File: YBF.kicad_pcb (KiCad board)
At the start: 2 copper layers, 173.9 x 130.1 mm, 119 parts, among them J1 Chain_LED_out, J2 Chain_LED_return, SW1 1825910-6, SW2 1825910-6

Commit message: Hieracrchical PCB
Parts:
- removed the C1 at (119.9, 134.1)
- removed the C3 at (46.5, 157.5)
- removed the C4 at (46.5, 160.0)
- removed the C5 at (46.5, 162.6)
- removed the C6 at (46.5, 165.1)
- removed the C7 at (46.5, 167.6)
- removed the C8 at (46.5, 170.2)
- added C100: 1uF, Capacitor_SMD:C_0603_1608Metric, F.Cu at (32.8, 260.4)
- added C101: 1uF, Capacitor_SMD:C_0603_1608Metric, F.Cu at (1.03, 236.2)
- added C102: 1uF, Capacitor_SMD:C_0603_1608Metric, F.Cu at (45.2, 260.4)
- added C103: 1uF, Capacitor_SMD:C_0603_1608Metric, F.Cu at (57.9, 252.2)
- added C104: 1uF, Capacitor_SMD:C_0603_1608Metric, F.Cu at (20.1, 260.4)
- added C53: 1uF, Capacitor_SMD:C_0603_1608Metric, F.Cu at (20.1, 220.0)
- added C54: 1uF, Capacitor_SMD:C_0603_1608Metric, F.Cu at (51.6, 228.1)
- added C55: 1uF, Capacitor_SMD:C_0603_1608Metric, F.Cu at (1.03, 260.4)
- added C56: 1uF, Capacitor_SMD:C_0603_1608Metric, F.Cu at (39.1, 252.2)
- added C57: 1uF, Capacitor_SMD:C_0603_1608Metric, F.Cu at (1.03, 276.4)
- added C58: 1uF, Capacitor_SMD:C_0603_1608Metric, F.Cu at (39.1, 244.1)
- added C59: 1uF, Capacitor_SMD:C_0603_1608Metric, F.Cu at (39.1, 268.5)
- added C60: 1uF, Capacitor_SMD:C_0603_1608Metric, F.Cu at (7.38, 284.5)
- added C61: 1uF, Capacitor_SMD:C_0603_1608Metric, F.Cu at (45.2, 220.0)
- added C62: 1uF, Capacitor_SMD:C_0603_1608Metric, F.Cu at (20.1, 236.2)
- added C63: 1uF, Capacitor_SMD:C_0603_1608Metric, F.Cu at (7.38, 228.1)
- added C64: 1uF, Capacitor_SMD:C_0603_1608Metric, F.Cu at (51.6, 276.4)
- added C65: 1uF, Capacitor_SMD:C_0603_1608Metric, F.Cu at (20.1, 268.5)
- added C66: 1uF, Capacitor_SMD:C_0603_1608Metric, F.Cu at (26.4, 252.2)
- added C67: 1uF, Capacitor_SMD:C_0603_1608Metric, F.Cu at (1.03, 252.2)
- added C68: 1uF, Capacitor_SMD:C_0603_1608Metric, F.Cu at (26.4, 260.4)
- added C69: 1uF, Capacitor_SMD:C_0603_1608Metric, F.Cu at (13.7, 260.4)
- added C70: 1uF, Capacitor_SMD:C_0603_1608Metric, F.Cu at (7.38, 260.4)
- added C71: 1uF, Capacitor_SMD:C_0603_1608Metric, F.Cu at (1.03, 220.0)
- added C72: 1uF, Capacitor_SMD:C_0603_1608Metric, F.Cu at (57.9, 268.5)
- added C73: 1uF, Capacitor_SMD:C_0603_1608Metric, F.Cu at (20.1, 244.1)
- added C74: 1uF, Capacitor_SMD:C_0603_1608Metric, F.Cu at (7.38, 276.4)
- added C75: 1uF, Capacitor_SMD:C_0603_1608Metric, F.Cu at (7.38, 236.2)
- added C76: 1uF, Capacitor_SMD:C_0603_1608Metric, F.Cu at (39.1, 260.4)
- added C77: 1uF, Capacitor_SMD:C_0603_1608Metric, F.Cu at (51.6, 244.1)
- added C78: 1uF, Capacitor_SMD:C_0603_1608Metric, F.Cu at (32.8, 244.1)
- added C79: 1uF, Capacitor_SMD:C_0603_1608Metric, F.Cu at (45.2, 252.2)
- added C80: 1uF, Capacitor_SMD:C_0603_1608Metric, F.Cu at (20.1, 228.1)
- added C81: 1uF, Capacitor_SMD:C_0603_1608Metric, F.Cu at (7.38, 268.5)
- added C82: 1uF, Capacitor_SMD:C_0603_1608Metric, F.Cu at (64.3, 236.2)
- added C83: 1uF, Capacitor_SMD:C_0603_1608Metric, F.Cu at (1.03, 228.1)
- added C84: 1uF, Capacitor_SMD:C_0603_1608Metric, F.Cu at (39.1, 236.2)
- added C85: 1uF, Capacitor_SMD:C_0603_1608Metric, F.Cu at (32.8, 276.4)
- added C86: 1uF, Capacitor_SMD:C_0603_1608Metric, F.Cu at (1.03, 244.1)
- added C87: 1uF, Capacitor_SMD:C_0603_1608Metric, F.Cu at (51.6, 260.4)
- added C88: 1uF, Capacitor_SMD:C_0603_1608Metric, F.Cu at (45.2, 284.5)
- added C89: 1uF, Capacitor_SMD:C_0603_1608Metric, F.Cu at (51.6, 236.2)
- added C90: 1uF, Capacitor_SMD:C_0603_1608Metric, F.Cu at (45.2, 228.1)
- added C91: 1uF, Capacitor_SMD:C_0603_1608Metric, F.Cu at (64.3, 268.5)
- added C92: 1uF, Capacitor_SMD:C_0603_1608Metric, F.Cu at (45.2, 268.5)
- added C93: 1uF, Capacitor_SMD:C_0603_1608Metric, F.Cu at (26.4, 228.1)
- added C94: 1uF, Capacitor_SMD:C_0603_1608Metric, F.Cu at (13.7, 276.4)
- added C95: 1uF, Capacitor_SMD:C_0603_1608Metric, F.Cu at (1.03, 284.5)
- added C96: 1uF, Capacitor_SMD:C_0603_1608Metric, F.Cu at (51.6, 220.0)
- added C97: 1uF, Capacitor_SMD:C_0603_1608Metric, F.Cu at (45.2, 236.2)
- added C98: 1uF, Capacitor_SMD:C_0603_1608Metric, F.Cu at (39.1, 228.1)
- added C99: 1uF, Capacitor_SMD:C_0603_1608Metric, F.Cu at (13.7, 236.2)
- added D2: WS2812B-2020, LED_SMD:LED_WS2812B-2020_PLCC4_2.0x2.0mm, F.Cu at (124.0, 152.4)
- added D53: WS2812B-2020, LED_SMD:LED_WS2812B-2020_PLCC4_2.0x2.0mm, F.Cu at (45.2, 222.2)
- added D54: WS2812B-2020, LED_SMD:LED_WS2812B-2020_PLCC4_2.0x2.0mm, F.Cu at (20.1, 238.5)
- added D55: WS2812B-2020, LED_SMD:LED_WS2812B-2020_PLCC4_2.0x2.0mm, F.Cu at (7.37, 230.4)
- added D56: WS2812B-2020, LED_SMD:LED_WS2812B-2020_PLCC4_2.0x2.0mm, F.Cu at (51.6, 278.6)
- added D57: WS2812B-2020, LED_SMD:LED_WS2812B-2020_PLCC4_2.0x2.0mm, F.Cu at (20.1, 270.8)
- added D58: WS2812B-2020, LED_SMD:LED_WS2812B-2020_PLCC4_2.0x2.0mm, F.Cu at (26.4, 254.5)
- added D59: WS2812B-2020, LED_SMD:LED_WS2812B-2020_PLCC4_2.0x2.0mm, F.Cu at (1.02, 254.5)
- added D60: WS2812B-2020, LED_SMD:LED_WS2812B-2020_PLCC4_2.0x2.0mm, F.Cu at (26.4, 262.6)
- added D61: WS2812B-2020, LED_SMD:LED_WS2812B-2020_PLCC4_2.0x2.0mm, F.Cu at (13.7, 262.6)
- added D62: WS2812B-2020, LED_SMD:LED_WS2812B-2020_PLCC4_2.0x2.0mm, F.Cu at (7.37, 262.6)
- added D63: WS2812B-2020, LED_SMD:LED_WS2812B-2020_PLCC4_2.0x2.0mm, F.Cu at (1.02, 222.2)
- added D64: WS2812B-2020, LED_SMD:LED_WS2812B-2020_PLCC4_2.0x2.0mm, F.Cu at (57.9, 270.8)
- added D65: WS2812B-2020, LED_SMD:LED_WS2812B-2020_PLCC4_2.0x2.0mm, F.Cu at (20.1, 246.4)
- added D66: WS2812B-2020, LED_SMD:LED_WS2812B-2020_PLCC4_2.0x2.0mm, F.Cu at (7.37, 278.6)
- added D67: WS2812B-2020, LED_SMD:LED_WS2812B-2020_PLCC4_2.0x2.0mm, F.Cu at (7.37, 238.5)
- added D68: WS2812B-2020, LED_SMD:LED_WS2812B-2020_PLCC4_2.0x2.0mm, F.Cu at (39.1, 262.6)
- added D69: WS2812B-2020, LED_SMD:LED_WS2812B-2020_PLCC4_2.0x2.0mm, F.Cu at (51.6, 246.4)
- added D70: WS2812B-2020, LED_SMD:LED_WS2812B-2020_PLCC4_2.0x2.0mm, F.Cu at (32.8, 246.4)
- added D71: WS2812B-2020, LED_SMD:LED_WS2812B-2020_PLCC4_2.0x2.0mm, F.Cu at (45.2, 254.5)
- added D72: WS2812B-2020, LED_SMD:LED_WS2812B-2020_PLCC4_2.0x2.0mm, F.Cu at (20.1, 230.4)
- added D73: WS2812B-2020, LED_SMD:LED_WS2812B-2020_PLCC4_2.0x2.0mm, F.Cu at (7.37, 270.8)
- added D74: WS2812B-2020, LED_SMD:LED_WS2812B-2020_PLCC4_2.0x2.0mm, F.Cu at (64.3, 238.5)
- added D75: WS2812B-2020, LED_SMD:LED_WS2812B-2020_PLCC4_2.0x2.0mm, F.Cu at (1.02, 230.4)
- added D76: WS2812B-2020, LED_SMD:LED_WS2812B-2020_PLCC4_2.0x2.0mm, F.Cu at (39.1, 238.5)
- added D77: WS2812B-2020, LED_SMD:LED_WS2812B-2020_PLCC4_2.0x2.0mm, F.Cu at (32.8, 278.6)
- added D78: WS2812B-2020, LED_SMD:LED_WS2812B-2020_PLCC4_2.0x2.0mm, F.Cu at (1.02, 246.4)
- added D79: WS2812B-2020, LED_SMD:LED_WS2812B-2020_PLCC4_2.0x2.0mm, F.Cu at (51.6, 262.6)
- added D80: WS2812B-2020, LED_SMD:LED_WS2812B-2020_PLCC4_2.0x2.0mm, F.Cu at (45.2, 286.8)
- added D81: WS2812B-2020, LED_SMD:LED_WS2812B-2020_PLCC4_2.0x2.0mm, F.Cu at (51.6, 238.5)
- added D82: WS2812B-2020, LED_SMD:LED_WS2812B-2020_PLCC4_2.0x2.0mm, F.Cu at (45.2, 230.4)
- added D83: WS2812B-2020, LED_SMD:LED_WS2812B-2020_PLCC4_2.0x2.0mm, F.Cu at (64.3, 270.8)
- added D84: WS2812B-2020, LED_SMD:LED_WS2812B-2020_PLCC4_2.0x2.0mm, F.Cu at (45.2, 270.8)
- added D85: WS2812B-2020, LED_SMD:LED_WS2812B-2020_PLCC4_2.0x2.0mm, F.Cu at (26.4, 230.4)
- added D86: WS2812B-2020, LED_SMD:LED_WS2812B-2020_PLCC4_2.0x2.0mm, F.Cu at (13.7, 278.6)
- added D87: WS2812B-2020, LED_SMD:LED_WS2812B-2020_PLCC4_2.0x2.0mm, F.Cu at (1.02, 286.8)
- added D88: WS2812B-2020, LED_SMD:LED_WS2812B-2020_PLCC4_2.0x2.0mm, F.Cu at (51.6, 222.2)
- added D89: WS2812B-2020, LED_SMD:LED_WS2812B-2020_PLCC4_2.0x2.0mm, F.Cu at (45.2, 238.5)
- added D90: WS2812B-2020, LED_SMD:LED_WS2812B-2020_PLCC4_2.0x2.0mm, F.Cu at (39.1, 230.4)
- added D91: WS2812B-2020, LED_SMD:LED_WS2812B-2020_PLCC4_2.0x2.0mm, F.Cu at (13.7, 238.5)
- added D92: WS2812B-2020, LED_SMD:LED_WS2812B-2020_PLCC4_2.0x2.0mm, F.Cu at (32.8, 262.6)
- added D93: WS2812B-2020, LED_SMD:LED_WS2812B-2020_PLCC4_2.0x2.0mm, F.Cu at (1.02, 238.5)
- added D94: WS2812B-2020, LED_SMD:LED_WS2812B-2020_PLCC4_2.0x2.0mm, F.Cu at (45.2, 262.6)
- added D95: WS2812B-2020, LED_SMD:LED_WS2812B-2020_PLCC4_2.0x2.0mm, F.Cu at (57.9, 254.5)
- added D96: WS2812B-2020, LED_SMD:LED_WS2812B-2020_PLCC4_2.0x2.0mm, F.Cu at (20.1, 262.6)
- moved C23 133.0 mm to (39.1, 284.5), turned to 180 degrees
- moved C14 132.2 mm to (13.7, 284.5), turned to 180 degrees
- moved C34 128.0 mm to (26.4, 276.4), turned to 180 degrees
- moved C48 128.0 mm to (32.8, 284.5), turned to 180 degrees
- moved D21 126.8 mm to (26.4, 286.8)
- moved C16 125.7 mm to (20.1, 284.5), turned to 180 degrees
- moved C15 124.5 mm to (51.6, 284.5), turned to 180 degrees
- moved D40 123.3 mm to (32.8, 286.8)
- moved D49 122.3 mm to (1.02, 278.6)
- moved C29 120.2 mm to (26.4, 284.5), turned to 180 degrees
- moved C25 118.3 mm to (13.7, 268.5), turned to 180 degrees
- moved D52 117.9 mm to (7.37, 286.8)
- moved D15 116.9 mm to (39.1, 286.8)
- moved D7 116.6 mm to (51.6, 286.8)
- moved C26 116.4 mm to (57.9, 276.4), turned to 180 degrees
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- renumbered C60 to C1, C53 to C2, C55 to C3, C59 to C4, C56 to C5, C58 to C6, C57 to C7, C54 to C8, U4 to U1, U1 to U2, U2 to U3
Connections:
- net Net-(D10-DIN) renamed /ws2812_and_cap8/DOUT
- net Net-(D10-DOUT) renamed /ws2812_and_cap10/DIN
- net Net-(D11-DOUT) renamed /ws2812_and_cap10/DOUT
- net Net-(D12-DOUT) renamed /ws2812_and_cap11/DOUT
- net Net-(D13-DOUT) renamed /ws2812_and_cap12/DOUT
- net Net-(D14-DOUT) renamed /ws2812_and_cap13/DOUT
- net Net-(D15-DOUT) renamed /ws2812_and_cap14/DOUT
- net Net-(D17-DOUT) renamed /ws2812_and_cap17/DOUT
- net Net-(D20-DOUT) renamed /ws2812_and_cap19/DOUT
- net Net-(D21-DOUT) renamed /ws2812_and_cap20/DOUT
- net Net-(D22-DOUT) renamed /ws2812_and_cap21/DOUT
- net Net-(D23-DOUT) renamed /ws2812_and_cap22/DOUT
- net Net-(D24-DOUT) renamed /ws2812_and_cap23/DOUT
- net Net-(D25-DOUT) renamed /ws2812_and_cap24/DOUT
- net Net-(D4-DOUT) renamed /ws2812_and_cap3/DOUT
- net Net-(D5-DOUT) renamed /ws2812_and_cap4/DOUT
- net Net-(D6-DOUT) renamed /ws2812_and_cap5/DOUT
- net Net-(D7-DOUT) renamed /ws2812_and_cap6/DOUT
- net Net-(D8-DOUT) renamed /ws2812_and_cap7/DOUT
- D1 pad 1: Net-(D1-DOUT) -> /ws2812_and_cap1/DOUT
- D1 pad 3: /Perimeter LEDs/DIN -> /ws2812_and_cap/DOUT
- D16 pad 1: Net-(D16-DOUT) -> /ws2812_and_cap15/DOUT
- D17 pad 3: Net-(D16-DOUT) -> /ws2812_and_cap16/DOUT
- D18 pad 1: Net-(D18-DOUT) -> /ws2812_and_cap18/DOUT
- D19 pad 1: Net-(D19-DOUT) -> /ws2812_and_cap16/DOUT
- D19 pad 3: Net-(D18-DOUT) -> /ws2812_and_cap15/DOUT
- D20 pad 3: Net-(D19-DOUT) -> /ws2812_and_cap18/DOUT
- D26 pad 1: Net-(D26-DOUT) -> /ws2812_and_cap25/DOUT
- D27 pad 1: Net-(D27-DOUT) -> /ws2812_and_cap26/DOUT
- D27 pad 3: Net-(D27-DIN) -> /ws2812_and_cap25/DOUT
- D28 pad 1: Net-(D27-DIN) -> /ws2812_and_cap27/DOUT
- D28 pad 3: Net-(D28-DIN) -> /ws2812_and_cap26/DOUT
- D29 pad 1: Net-(D28-DIN) -> /ws2812_and_cap28/DOUT
- D29 pad 3: Net-(D29-DIN) -> /ws2812_and_cap27/DOUT
- D3 pad 1: Net-(D3-DOUT) -> /ws2812_and_cap/DOUT
- D3 pad 3: Net-(D2-DOUT) -> PERIM_LED_DATA_IN
- D30 pad 1: Net-(D29-DIN) -> /ws2812_and_cap29/DOUT
- D30 pad 3: Net-(D30-DIN) -> /ws2812_and_cap28/DOUT
- D31 pad 1: Net-(D30-DIN) -> /ws2812_and_cap30/DOUT
- D31 pad 3: Net-(D31-DIN) -> /ws2812_and_cap29/DOUT
- D32 pad 1: Net-(D31-DIN) -> /ws2812_and_cap31/DOUT
- D32 pad 3: Net-(D32-DIN) -> /ws2812_and_cap30/DOUT
- D33 pad 1: Net-(D32-DIN) -> /ws2812_and_cap33/DOUT
- D33 pad 3: Net-(D33-DIN) -> /ws2812_and_cap32/DOUT
- D34 pad 1: Net-(D33-DIN) -> /ws2812_and_cap34/DOUT
- D34 pad 3: Net-(D34-DIN) -> /ws2812_and_cap33/DOUT
- D35 pad 1: Net-(D34-DIN) -> /ws2812_and_cap32/DOUT
- D35 pad 3: Net-(D35-DIN) -> /ws2812_and_cap31/DOUT
- D36 pad 1: Net-(D35-DIN) -> /ws2812_and_cap35/DOUT
- D36 pad 3: Net-(D36-DIN) -> /ws2812_and_cap34/DOUT
- D37 pad 1: Net-(D36-DIN) -> /ws2812_and_cap36/DOUT
- D37 pad 3: Net-(D37-DIN) -> /ws2812_and_cap35/DOUT
- D38 pad 1: Net-(D37-DIN) -> /ws2812_and_cap37/DOUT
- D38 pad 3: Net-(D38-DIN) -> /ws2812_and_cap36/DOUT
- D39 pad 1: Net-(D38-DIN) -> /ws2812_and_cap38/DOUT
- D39 pad 3: Net-(D26-DOUT) -> /ws2812_and_cap37/DOUT
- D4 pad 3: Net-(D3-DOUT) -> /ws2812_and_cap2/DOUT
- D40 pad 1: /DATA_CHAIN_OUT -> /ws2812_and_cap39/DOUT
- D40 pad 3: Net-(D40-DIN) -> /ws2812_and_cap38/DOUT
- D41 pad 1: Net-(D40-DIN) -> /ws2812_and_cap40/DOUT
- D41 pad 3: Net-(D41-DIN) -> /ws2812_and_cap39/DOUT
- D42 pad 1: Net-(D41-DIN) -> /ws2812_and_cap41/DOUT
- D42 pad 3: Net-(D42-DIN) -> /ws2812_and_cap40/DOUT
- D43 pad 1: Net-(D42-DIN) -> /ws2812_and_cap42/DOUT
- D43 pad 3: Net-(D43-DIN) -> /ws2812_and_cap41/DOUT
- D44 pad 1: Net-(D43-DIN) -> /ws2812_and_cap43/DOUT
- D44 pad 3: Net-(D44-DIN) -> /ws2812_and_cap42/DOUT
- D45 pad 1: Net-(D44-DIN) -> /ws2812_and_cap44/DOUT
- D45 pad 3: Net-(D45-DIN) -> /ws2812_and_cap43/DOUT
- D46 pad 1: Net-(D45-DIN) -> /ws2812_and_cap45/DOUT
- D46 pad 3: Net-(D46-DIN) -> /ws2812_and_cap44/DOUT
- D47 pad 1: Net-(D46-DIN) -> /ws2812_and_cap46/DOUT
- D47 pad 3: Net-(D47-DIN) -> /ws2812_and_cap45/DOUT
- D48 pad 1: Net-(D47-DIN) -> /ws2812_and_cap47/DOUT
- D48 pad 3: Net-(D48-DIN) -> /ws2812_and_cap46/DOUT
- D49 pad 1: Net-(D48-DIN) -> /ws2812_and_cap48/DOUT
- D49 pad 3: Net-(D49-DIN) -> /ws2812_and_cap47/DOUT
- D50 pad 1: Net-(D49-DIN) -> /ws2812_and_cap49/DOUT
- D50 pad 3: Net-(D50-DIN) -> /ws2812_and_cap48/DOUT
- D51 pad 1: Net-(D50-DIN) -> /ws2812_and_cap50/DOUT
- D51 pad 3: Net-(D51-DIN) -> /ws2812_and_cap49/DOUT
- D52 pad 1: Net-(D51-DIN) -> /ws2812_and_cap51/DOUT
- D52 pad 3: Net-(D27-DOUT) -> /ws2812_and_cap50/DOUT
- J1 pad 2: /DATA_CHAIN_OUT -> PERIM_LED_DATA_IN
- U2 pad 5: /Perimeter LEDs/DIN -> PERIM_LED_DATA_OUT
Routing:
- net GND: track 1.54 -> 427.6 mm, vias 0 -> 96
- net Vdrive: track 3.68 -> 171.7 mm
- net /ws2812_and_cap70/DOUT: track 0.00 -> 4.67 mm
- net /ws2812_and_cap10/DIN: track 0.00 -> 4.67 mm
- net /ws2812_and_cap84/DOUT: track 0.00 -> 4.67 mm
- net /ws2812_and_cap54/DOUT: track 0.00 -> 4.67 mm
- net /ws2812_and_cap47/DOUT: track 0.00 -> 4.67 mm
- net /ws2812_and_cap83/DOUT: track 0.00 -> 4.67 mm
- net /ws2812_and_cap65/DOUT: track 0.00 -> 4.67 mm
- net /ws2812_and_cap31/DOUT: track 0.00 -> 4.67 mm
- net /ws2812_and_cap57/DOUT: track 0.00 -> 4.67 mm
- net /ws2812_and_cap8/DOUT: track 0.00 -> 4.67 mm
- net /ws2812_and_cap24/DOUT: track 0.00 -> 4.67 mm
- net /ws2812_and_cap33/DOUT: track 0.00 -> 4.67 mm
- net /ws2812_and_cap20/DOUT: track 0.00 -> 4.67 mm
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
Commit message: place perim LEDs
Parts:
- removed C100, C101, C102, C103, C104, C79, C80, C81, C82, C83, C84, C85, C86, C87, C88, C89, C90, C91, C92, C93, C94, C95, C96, C97, C98, C99: 1uF, Capacitor_SMD:C_0603_1608Metric
- removed D71, D72, D73, D74, D75, D76, D77, D78, D79, D80, D81, D82, D83, D84, D85, D86, D87, D88, D89, D90, D91, D92, D93, D94, D95, D96: WS2812B-2020, LED_SMD:LED_WS2812B-2020_PLCC4_2.0x2.0mm
- moved C60 291.8 mm to (201.4, 66.5)
- moved D52 291.8 mm to (201.4, 68.8)
- moved D49 270.3 mm to (193.3, 88.6)
- moved C57 270.3 mm to (193.3, 86.4)
- moved C74 262.6 mm to (220.9, 123.4)
- moved D66 262.6 mm to (220.9, 125.7)
- moved D40 262.5 mm to (159.5, 56.9), turned to 180 degrees
- moved C48 258.5 mm to (159.5, 59.2), turned to 0 degrees
- moved D38 258.3 mm to (157.3, 39.8), turned to 180 degrees
- moved C42 257.6 mm to (136.5, 37.8)
- moved D34 257.6 mm to (136.4, 40.1)
- moved C46 254.5 mm to (157.3, 42.1), turned to 0 degrees
- moved C59 251.9 mm to (198.4, 73.4)
- moved D51 251.9 mm to (198.4, 75.7)
- moved D36 251.6 mm to (141.0, 33.2), turned to -90 degrees
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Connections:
- D70 pad 1: /ws2812_and_cap69/DOUT -> PERIM_LED_DATA_OUT
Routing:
- net GND: track 427.6 -> 311.8 mm, vias 96 -> 70
- net Vdrive: track 171.7 -> 125.2 mm
- net /ws2812_and_cap70/DOUT: track 4.67 -> 0.00 mm
- net /ws2812_and_cap84/DOUT: track 4.67 -> 0.00 mm
- net /ws2812_and_cap83/DOUT: track 4.67 -> 0.00 mm
- net /ws2812_and_cap93/DOUT: track 4.67 -> 0.00 mm
- net /ws2812_and_cap94/DOUT: track 4.67 -> 0.00 mm
- net /ws2812_and_cap69/DOUT: track 4.67 -> 0.00 mm
- net /ws2812_and_cap78/DOUT: track 4.67 -> 0.00 mm
- net /ws2812_and_cap88/DOUT: track 4.67 -> 0.00 mm
- net /ws2812_and_cap85/DOUT: track 4.67 -> 0.00 mm
- net /ws2812_and_cap80/DOUT: track 4.67 -> 0.00 mm
- net /ws2812_and_cap89/DOUT: track 4.67 -> 0.00 mm
- net /ws2812_and_cap73/DOUT: track 4.67 -> 0.00 mm
- net /ws2812_and_cap72/DOUT: track 4.67 -> 0.00 mm
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
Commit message: routing progress
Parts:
- moved C11 12.4 mm to (127.3, 153.2)
- moved D3 12.4 mm to (129.6, 153.2)
- moved C9 7.28 mm to (121.2, 152.4)
- moved D1 7.28 mm to (123.4, 152.4)
- moved D2 6.90 mm to (118.2, 148.7)
- moved C10 6.90 mm to (115.9, 148.6)
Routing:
- net Vdrive: track 125.2 -> 320.7 mm
- net Net-(U2-37): track 0.00 -> 150.0 mm, vias 0 -> 2
- net GND: track 311.8 -> 446.0 mm
- net /ws2812_and_cap12/DOUT: track 4.41 -> 67.8 mm, vias 0 -> 2
- net /ws2812_and_cap26/DOUT: track 4.41 -> 12.5 mm
- net /ws2812_and_cap2/DOUT: track 4.41 -> 10.6 mm
- net /ws2812_and_cap3/DOUT: track 4.41 -> 9.41 mm
- net /ws2812_and_cap4/DOUT: track 4.41 -> 9.01 mm
- net /ws2812_and_cap17/DOUT: track 4.41 -> 8.90 mm
- net /ws2812_and_cap1/DOUT: track 4.41 -> 8.68 mm
- net /ws2812_and_cap16/DOUT: track 4.41 -> 8.41 mm
- net /ws2812_and_cap19/DOUT: track 4.41 -> 8.21 mm
- net /ws2812_and_cap15/DOUT: track 4.41 -> 7.93 mm
- net /ws2812_and_cap6/DOUT: track 4.41 -> 7.78 mm
- net /ws2812_and_cap24/DOUT: track 4.41 -> 7.76 mm
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
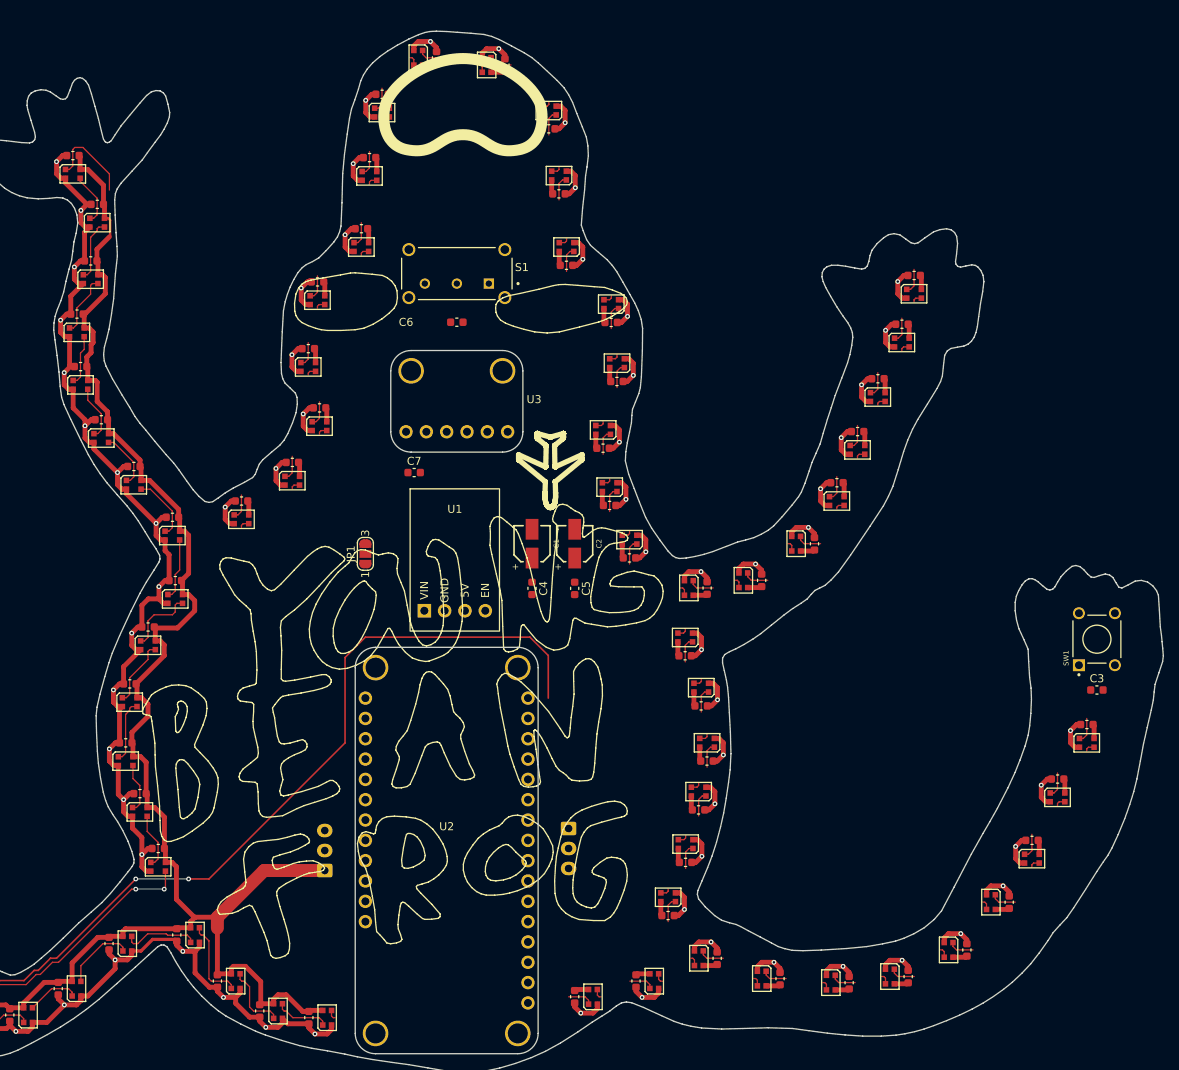
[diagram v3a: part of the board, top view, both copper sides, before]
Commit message: finish LED routing
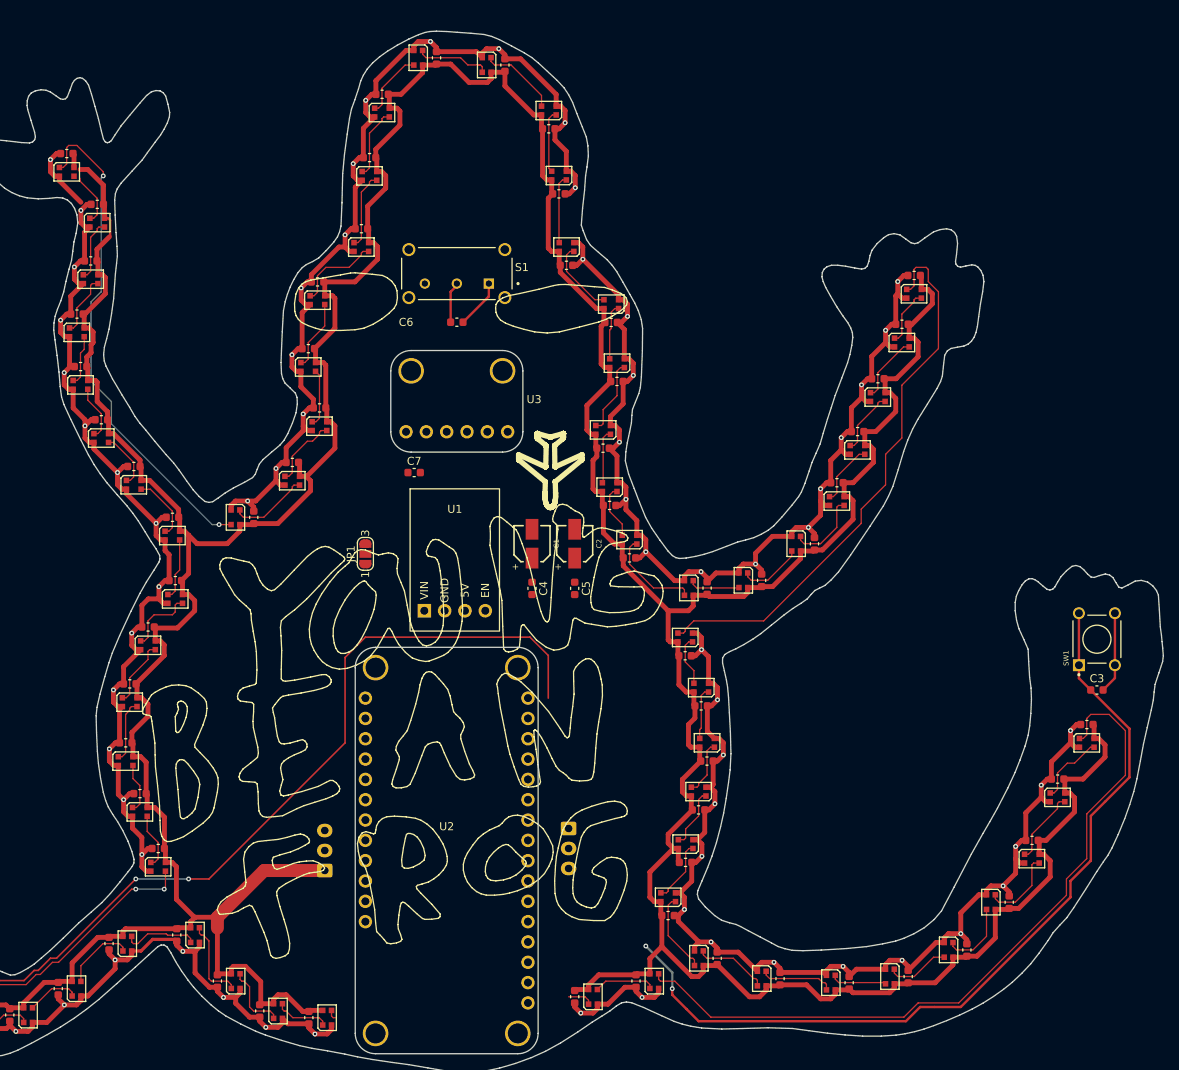
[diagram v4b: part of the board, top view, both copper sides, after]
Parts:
- moved C36 2.55 mm to (120.4, 90.7), turned to 90 degrees
- moved D27 0.80 mm to (97.0, 47.5)
- moved C35 0.80 mm to (97.0, 45.2)
- moved D28 0.79 mm to (118.1, 90.7), turned to -90 degrees
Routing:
- net Vdrive: track 320.7 -> 668.3 mm
- net GND: track 446.0 -> 674.9 mm
- net Net-(U2-27): track 0.00 -> 106.2 mm, vias 0 -> 2
- net /ws2812_and_cap67/DOUT: track 4.41 -> 92.6 mm
- net /ws2812_and_cap52/DOUT: track 4.41 -> 70.2 mm
- net /ws2812_and_cap26/DOUT: track 12.5 -> 62.6 mm, vias 0 -> 2
- net /ws2812_and_cap44/DOUT: track 4.41 -> 12.0 mm
- net /ws2812_and_cap31/DOUT: track 4.41 -> 11.0 mm
- net ~{DISABLE}: track 0.00 -> 6.16 mm
- net /ws2812_and_cap58/DOUT: track 4.41 -> 10.2 mm
- net /ws2812_and_cap27/DOUT: track 4.41 -> 9.94 mm
- net /ws2812_and_cap36/DOUT: track 4.41 -> 9.89 mm
- net /ws2812_and_cap64/DOUT: track 4.41 -> 9.69 mm
- net /ws2812_and_cap32/DOUT: track 4.41 -> 9.66 mm
- net /ws2812_and_cap47/DOUT: track 4.41 -> 9.57 mm
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
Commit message: more routing
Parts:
- moved J1 30.9 mm to (129.3, 134.8), turned to 90 degrees
- moved J2 30.9 mm to (159.8, 129.6), turned to -90 degrees
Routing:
- net +3.3V: track 0.00 -> 76.5 mm, vias 0 -> 2
- net +5V: track 0.00 -> 44.0 mm
- net PERIM_LED_DATA_OUT: track 3.16 -> 45.3 mm
- net +BATT: track 0.00 -> 33.7 mm
- net GND: track 674.9 -> 701.7 mm, vias 70 -> 79
- net Vdrive: track 668.3 -> 693.2 mm
- net PERIM_LED_DATA_IN: track 1.26 -> 25.1 mm
- net Net-(U2-37): track 150.0 -> 151.8 mm
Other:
- board text added: "5v"
- board text added: "VBAT"
- board text added: "WS2812 Vbus"

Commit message: v0.0.1
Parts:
- moved C5 34.8 mm to (125.7, 99.1), turned to 90 degrees
- moved C2 31.4 mm to (129.3, 97.3)
- moved C1 20.0 mm to (135.4, 97.0)
- moved C4 16.3 mm to (138.9, 99.1), turned to 90 degrees
- moved JP1 14.6 mm to (126.0, 107.2), turned to -90 degrees
- moved U1 12.2 mm to (145.5, 90.2), turned to 180 degrees
- moved J1 2.29 mm to (127.0, 134.8)
- moved D70 0.57 mm to (162.6, 150.1)
- moved C78 0.56 mm to (160.3, 150.1)
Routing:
- net ~{DISABLE}: track 6.16 -> 109.2 mm, vias 0 -> 4
- net Net-(U2-37): track 151.8 -> 89.7 mm
- net Net-(U2-15): track 0.00 -> 59.4 mm, vias 0 -> 2
- net Net-(U2-14): track 0.00 -> 53.1 mm, vias 0 -> 2
- net Net-(U2-SCL): track 0.00 -> 52.6 mm, vias 0 -> 2
- net Net-(U2-27): track 106.2 -> 157.8 mm, vias 2 -> 1
- net +BATT: track 33.7 -> 72.1 mm
- net +3.3V: track 76.5 -> 90.9 mm, vias 2 -> 1
- net +5V: track 44.0 -> 32.8 mm
- net PERIM_LED_DATA_OUT: track 45.3 -> 39.8 mm
- net GND: track 701.7 -> 696.4 mm, vias 79 -> 76
- net PERIM_LED_DATA_IN: track 25.1 -> 22.0 mm
- net Vdrive: track 693.2 -> 696.1 mm
- net /ws2812_and_cap26/DOUT: track 62.6 -> 61.6 mm
- net /ws2812_and_cap25/DOUT: track 6.54 -> 7.19 mm

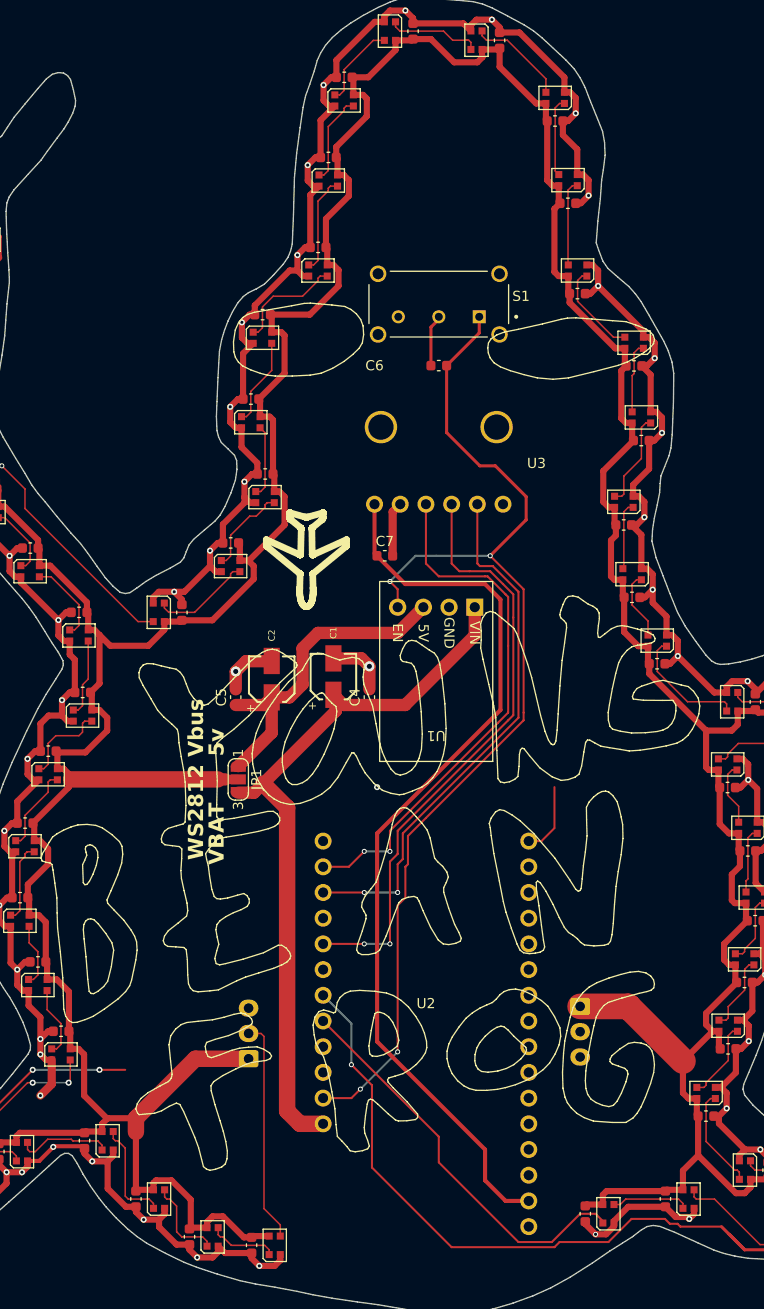
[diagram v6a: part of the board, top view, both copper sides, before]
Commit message: v0.0.2
add mounting holes and seperate chain and perim led lines
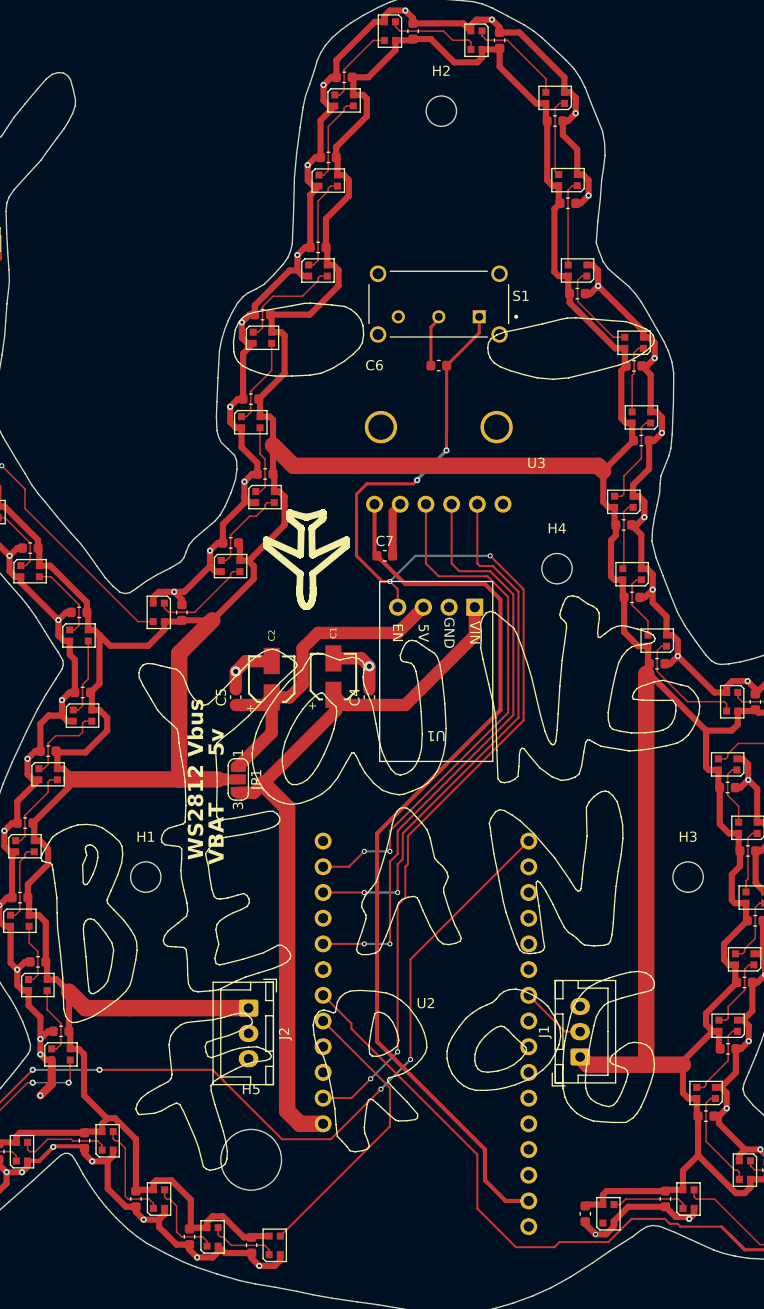
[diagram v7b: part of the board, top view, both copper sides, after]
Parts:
- added H1: MountingHole, MountingHole:MountingHole_3mm, F.Cu at (116.8, 116.8)
- added H2: MountingHole, MountingHole:MountingHole_3mm, F.Cu at (146.1, 41.1)
- added H3: MountingHole, MountingHole:MountingHole_3mm, F.Cu at (170.4, 116.8)
- added H4: MountingHole, MountingHole:MountingHole_3mm, F.Cu at (157.5, 86.4)
- added H5: MountingHole, MountingHole:MountingHole_6mm, F.Cu at (127.3, 144.8)
- J1, J2: moved to F.Cu
- moved J1 32.8 mm to (159.8, 134.6)
- moved J2 32.8 mm to (127.0, 129.8)
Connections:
- D70 pad 1: PERIM_LED_DATA_OUT -> /PERIM_LED_DATA_OUT
- J1 pad 2: PERIM_LED_DATA_IN -> /DATA_CHAIN_OUT
- U2 pad 19: unconnected-(U2-A5-Pad19) -> /DATA_CHAIN_OUT
- U2 pad 5: PERIM_LED_DATA_OUT -> PERIM_LED_DATA_IN
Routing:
- net Vdrive: track 696.1 -> 787.3 mm
- net Net-(U2-37): track 89.7 -> 143.3 mm, vias 2 -> 4
- net PERIM_LED_DATA_OUT: track 39.8 -> 0.00 mm
- net /DATA_CHAIN_OUT: track 0.00 -> 6.57 mm
- net PERIM_LED_DATA_IN: track 22.0 -> 28.5 mm
- net ~{DISABLE}: track 109.2 -> 114.3 mm, vias 4 -> 6
- net Net-(U2-27): track 157.8 -> 154.0 mm, vias 1 -> 0
- net +3.3V: vias 1 -> 0
